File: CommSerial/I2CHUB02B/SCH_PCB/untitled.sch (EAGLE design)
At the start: 46 parts, among them X1 TCA9548A, X2 SROUB3M, X3 SROUB3M, X4 SROUB3M, X5 SROUB3M, X6 LM1117-3.3

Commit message: 
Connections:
- net N$20 renamed A0
- net N$22 renamed A1
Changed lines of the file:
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@@
 <setting verticaltext="up"/>
 </settings>
-<grid distance="0.05" unitdist="inch" unit="inch" style="lines" multiple="1" display="no" altdistance="0.01" altunitdist="inch" altunit="inch"/>
+<grid distance="0.1" unitdist="inch" unit="inch" style="lines" multiple="1" display="no" altdistance="0.01" altunitdist="inch" altunit="inch"/>
 <layers>
 <layer number="1" name="Top" color="4" fill="1" visible="no" active="no"/>
@@
 </segment>
 </net>
-<net name="N$20" class="0">
+<net name="A0" class="0">
 <segment>
 <pinref part="X1" gate="G$1" pin="A0"/>
@@
 </segment>
 </net>
-<net name="N$22" class="0">
+<net name="A1" class="0">
 <segment>
 <pinref part="X1" gate="G$1" pin="A1"/>

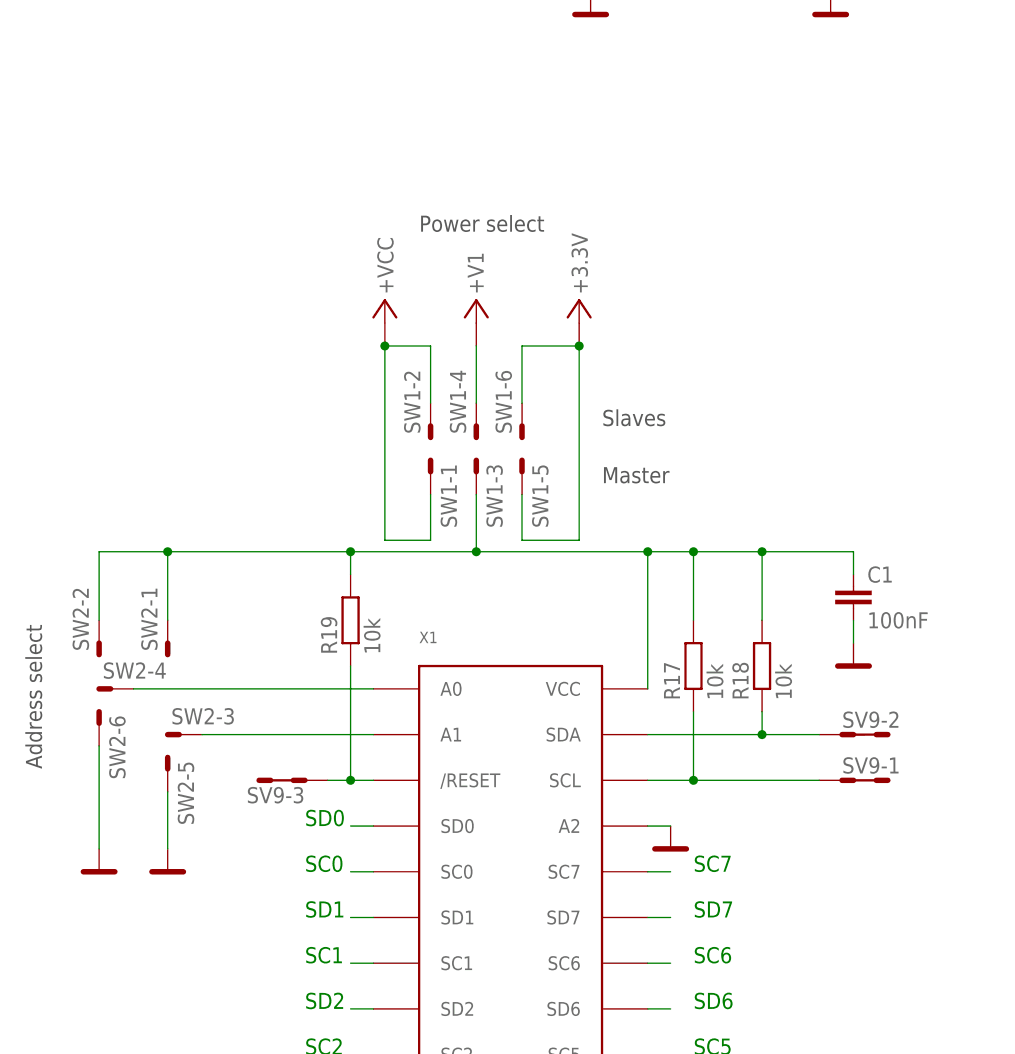
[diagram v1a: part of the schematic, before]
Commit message: 
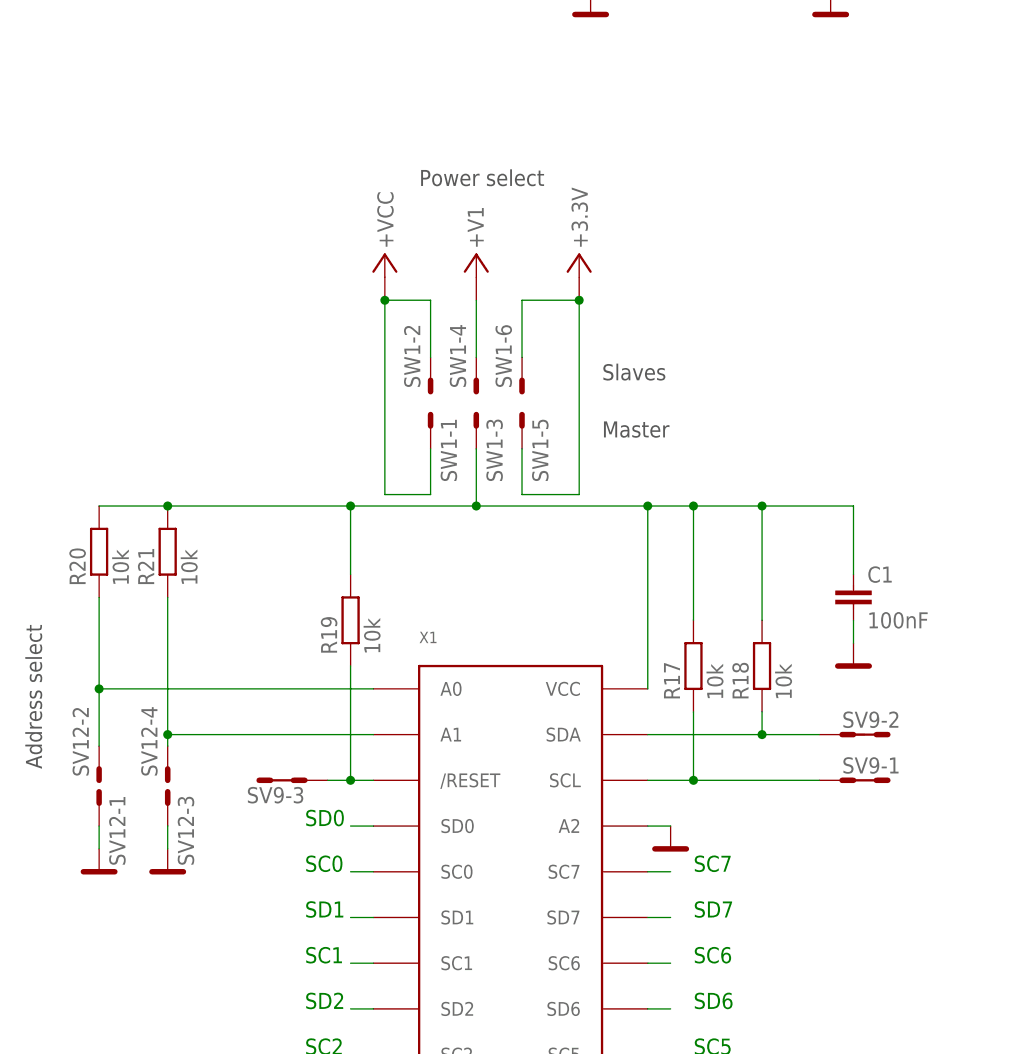
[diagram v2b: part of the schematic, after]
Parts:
- removed SW2: (no value), moje_hrebinky:MA03-3
- added R20, R21: 10k, moje_R:R0805
- added SV12: (no value), moje_hrebinky:MA02-3
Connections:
- removed net A1: SW2-3.P$1, X1.A1
- new net N$2: R21.1, SV12-4.P$1, X1.A1
- net A0: now also R20.1, SV12-2.P$1; no longer SW2-4.P$1
- net GND: now also SV12-1.P$1, SV12-3.P$1; no longer SW2-5.P$1, SW2-6.P$1
- net N$5: now also R20.2, R21.2; no longer SW2-1.P$1, SW2-2.P$1
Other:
- moved on the sheet: SW1-1, SW1-2, SW1-3, SW1-4, SW1-5, SW1-6
